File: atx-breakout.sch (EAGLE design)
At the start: 74 parts, among them Q1 IRF9530, Q2 IRF9530, Q3 IRF9530, Q4 IRF9530, Q5 IRF9530, Q6 IRF9530, T1 2N3904, T2 2N3904, T3 2N3904, T4 2N3904, T5 2N3904, T6 2N3904, X10 MA02-1JC, X12 XT30-J, X13 MA02-1JC, X15 XT30-J, X16 MA02-1JC, X2 XT30-J, X3 MA02-1JC, X4 XT30-J, X5 MA02-1JC, X6 XT30-J, X7 MA02-1JC, X9 XT30-J

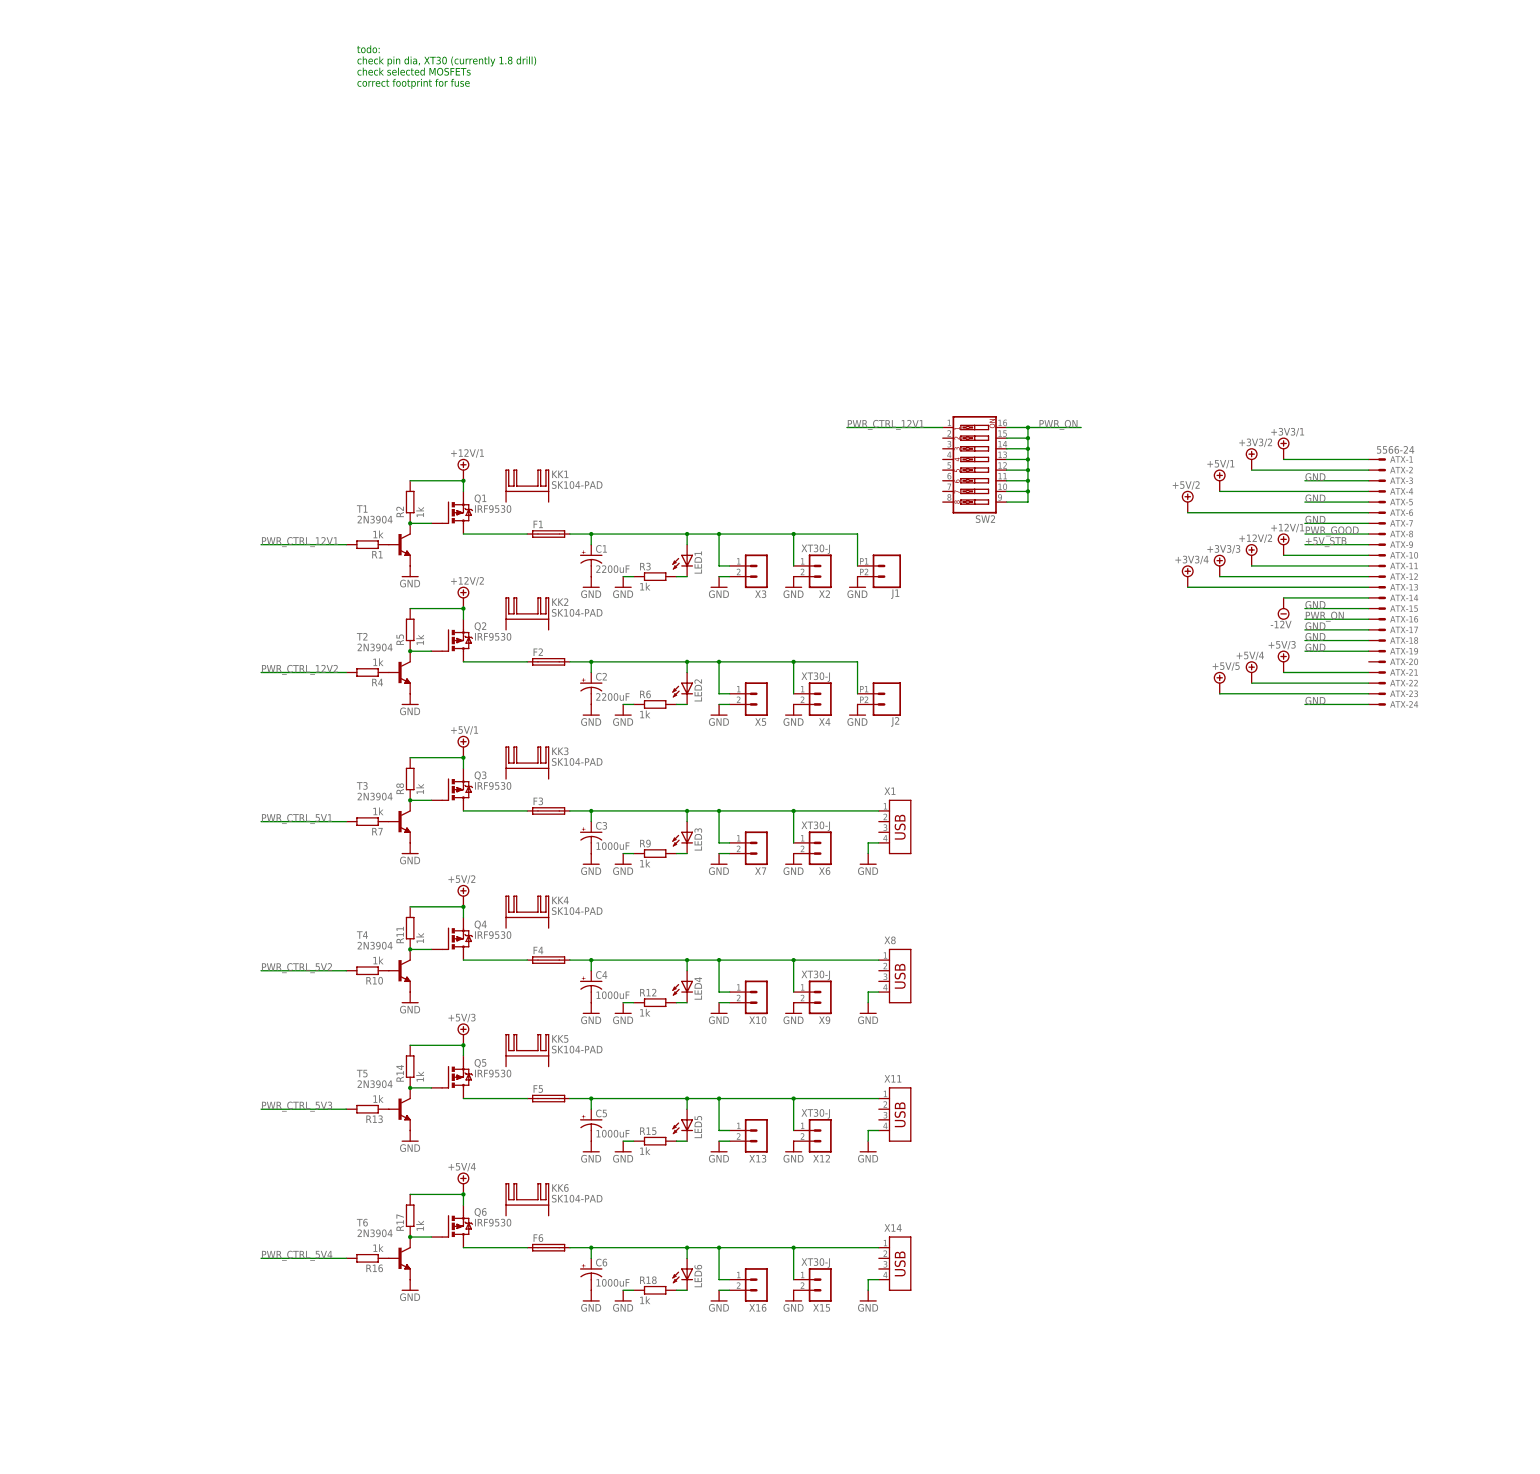
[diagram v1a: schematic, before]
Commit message: Added 3v3, control header, fan control headers, extra room for filter cap
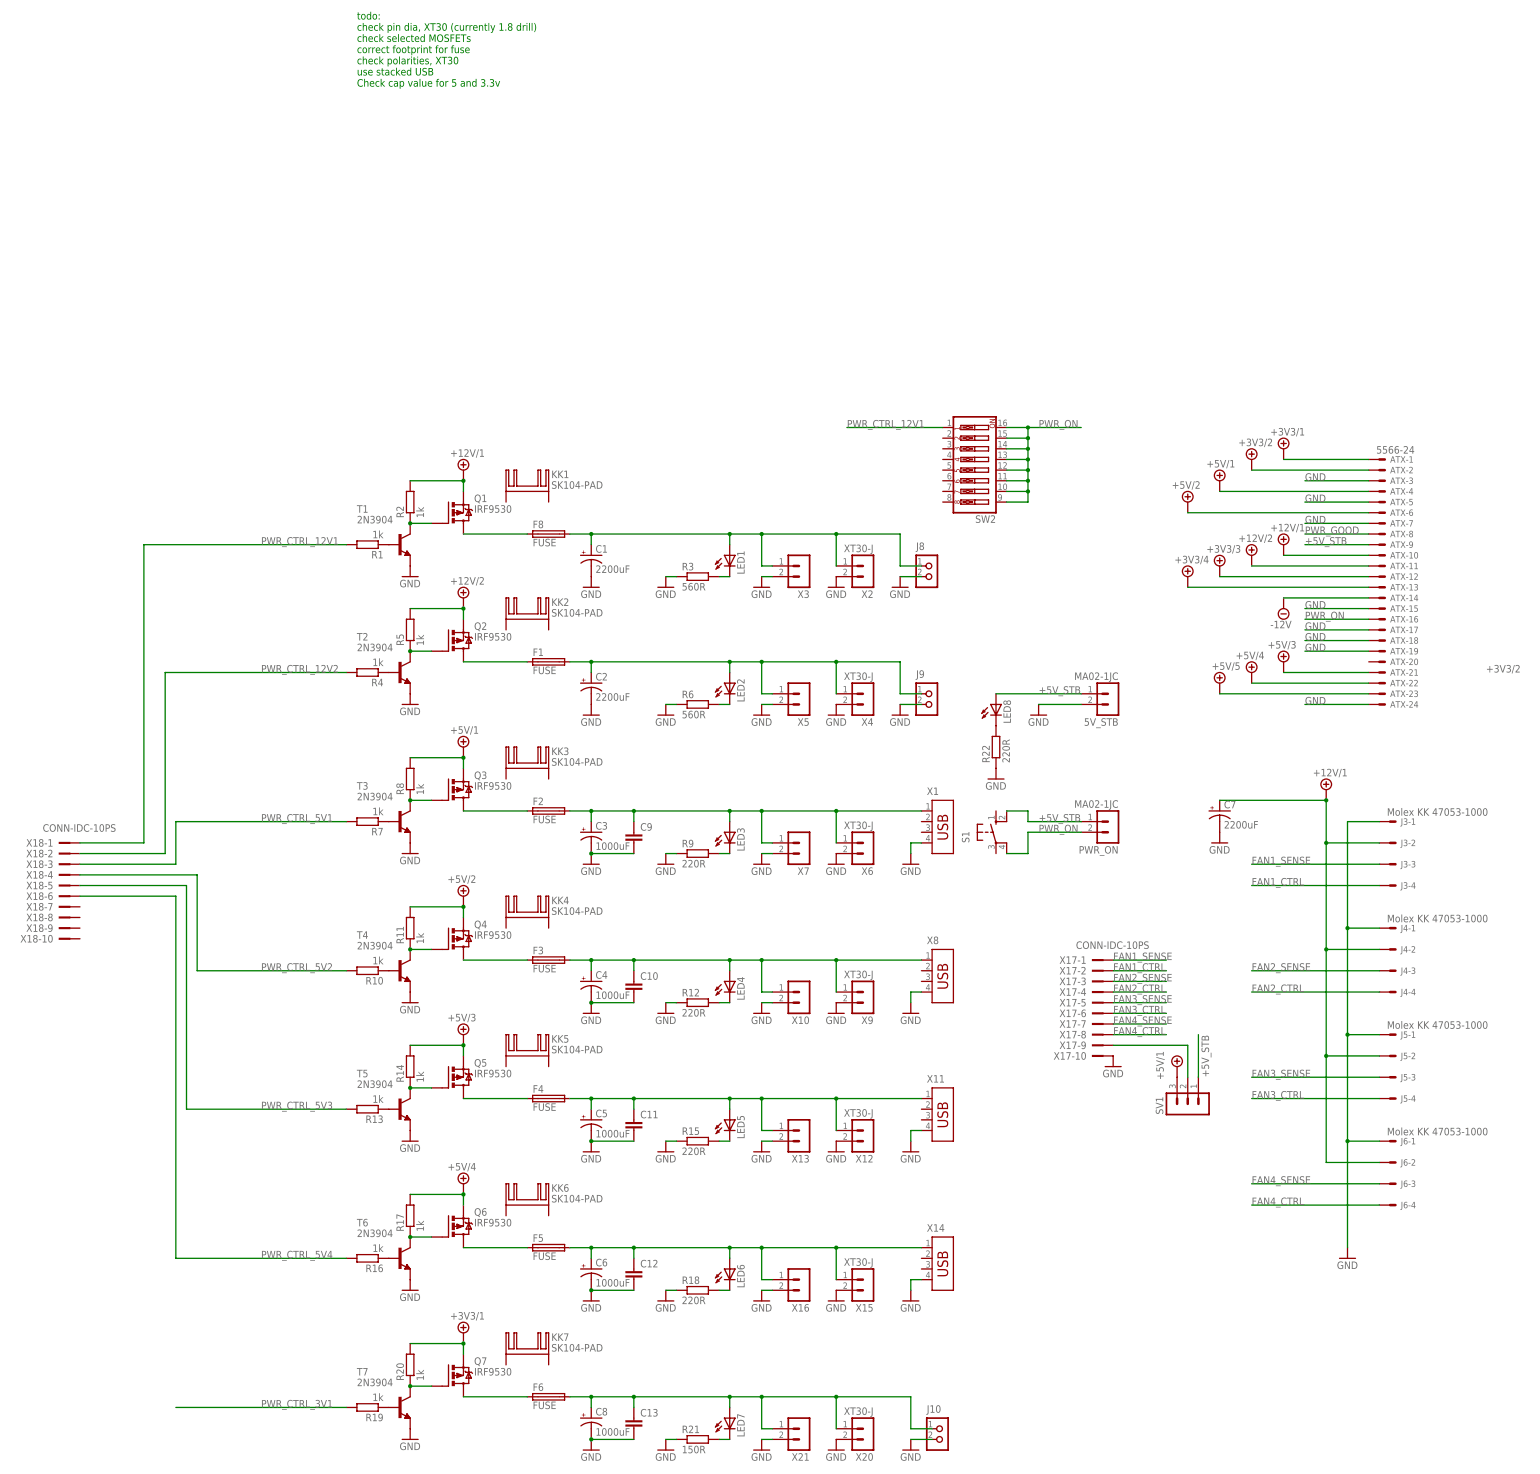
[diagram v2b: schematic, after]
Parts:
- removed J1, J2: (no value), SparkFun-Connectors:CONN_022.54MM_SCREWTERM
- added 5V_STB, PWR_ON, X21: MA02-1JC, joakim:MA02-1JC
- added C10, C11, C12, C13, C9: (no value), rcl:C-EU050-030X075
- added C7: 2200uF, rcl:CPOL-USE7.5-16
- added C8: 1000uF, rcl:CPOL-USE5-10.5
- added F8: FUSE, fuse:FUSEBLANK_5X20MM
- added J10, J8, J9: CON_TERMINAL_BLOCK_02-5MM, dp_devices.v6:CON_TERMINAL_BLOCK_02-5MM
- added J3, J4, J5, J6: Molex KK 47053-1000, con-molex:22-27-2041-04
- added KK7: SK104-PAD, heatsink:SK104-PAD
- added LED7, LED8: (no value), joakim:LED_J3MM
- added Q7: IRF9530, transistor-power:IRF9530
- added R19, R20: 1k, rcl:R-EU_0207/7
- added R21: 150R, rcl:R-EU_0207/7
- added R22: 220R, rcl:R-EU_0207/7
- added S1: (no value), joakim:PUSHBUTTON_12MM
- added SV1: (no value), joakim:MA03-1JC
- added T7: 2N3904, transistor:2N3904
- added X17, X18: CONN-IDC-10PS, joakim:CONN-IDC-10PS
- added X20: XT30-J, joakim:XT30-J
- F1, F2, F3, F4, F5, F6: value (none) -> FUSE; device fuse:LITTLEFUSE -> fuse:FUSEBLANK_5X20MM
- R12, R15, R18, R9: value 1k -> 220R
- R3, R6: value 1k -> 560R
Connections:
- new net +12V/1: ATX-10.S, C7.+, J3-2.S, J4-2.S, J5-2.S, J6-2.S, Q1.S, R2.2
- new net +12V/2: ATX-11.S, Q2.S, R5.2
- new net +3V3/1: ATX-1.S, Q7.S, R20.2
- new net +3V3/2: ATX-2.S
- new net +3V3/3: ATX-12.S
- new net +3V3/4: ATX-13.S
- new net FAN1_CTRL: J3-4.S, X17-2.KL
- new net FAN1_SENSE: J3-3.S, X17-1.KL
- new net FAN2_CTRL: J4-4.S, X17-4.KL
- new net FAN2_SENSE: J4-3.S, X17-3.KL
- new net FAN3_CTRL: J5-4.S, X17-6.KL
- new net FAN3_SENSE: J5-3.S, X17-5.KL
- new net FAN4_CTRL: J6-4.S, X17-8.KL
- new net FAN4_SENSE: J6-3.S, X17-7.KL
- new net N$32: SV1.2, X17-9.KL
- new net N$33: R19.1, T7.B
- new net N$34: Q7.G, R20.1, T7.C
- new net N$35: C13.1, C8.+, F6.2, J10.1, LED7.A, X20.1, X21.1
- new net N$36: LED7.C, R21.2
- new net N$37: F6.1, Q7.D
- new net PWR_CTRL_3V1: R19.2
- net +5V/1: now also SV1.3; no longer ATX-1.S, ATX-10.S, ATX-11.S, ATX-12.S, ATX-13.S, ATX-2.S, Q2.S, R5.2
- net +5V_STB: now also 5V_STB.1, LED8.A, PWR_ON.1, S1.S1, SV1.1
- net GND: now also 5V_STB.2, C10.2, C11.2, C12.2, C13.2, C7.-, C8.-, C9.2, J10.2, J3-1.S, J4-1.S, J5-1.S, J6-1.S, J8.2, J9.2, R21.1, R22.1, T7.E, X17-10.KL, X20.2, X21.2; no longer J1.2, J2.2
- net N$11: now also F1.1; no longer F2.1
- net N$14: now also C9.1, F2.2; no longer F3.2
- net N$16: now also F2.1; no longer F3.1
- net N$19: now also C10.1, F3.2; no longer F4.2
- net N$21: now also F3.1; no longer F4.1
- net N$24: now also C11.1, F4.2; no longer F5.2
- net N$26: now also F4.1; no longer F5.1
- net N$29: now also C12.1, F5.2; no longer F6.2
- net N$3: now also LED8.C, R22.2; no longer Q1.S, R2.2
- net N$31: now also F5.1; no longer F6.1
- net N$4: now also F8.2, J8.1; no longer F1.2, J1.1
- net N$6: now also F8.1; no longer F1.1
- net N$9: now also F1.2, J9.1; no longer F2.2, J2.1
- net PWR_CTRL_12V1: now also X18-1.KL
- net PWR_CTRL_12V2: now also X18-2.KL
- net PWR_CTRL_5V1: now also X18-3.KL
- net PWR_CTRL_5V2: now also X18-4.KL
- net PWR_CTRL_5V3: now also X18-5.KL
- net PWR_CTRL_5V4: now also X18-6.KL
- net PWR_ON: now also PWR_ON.2, S1.P1
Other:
- note added: "todo: check pin dia, XT30 (currently 1.8 drill) check selected MOSFETs correct footprint for fuse check polarities, XT30 use stacked USB Check cap value for 5 and 3.3v"
- note removed: "todo: check pin dia, XT30 (currently 1.8 drill) check selected MOSFETs correct footprint for fuse"
- moved on the sheet: LED1, LED2, LED3, LED4, LED5, LED6, R12, R15, R18, R3, R6, R9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

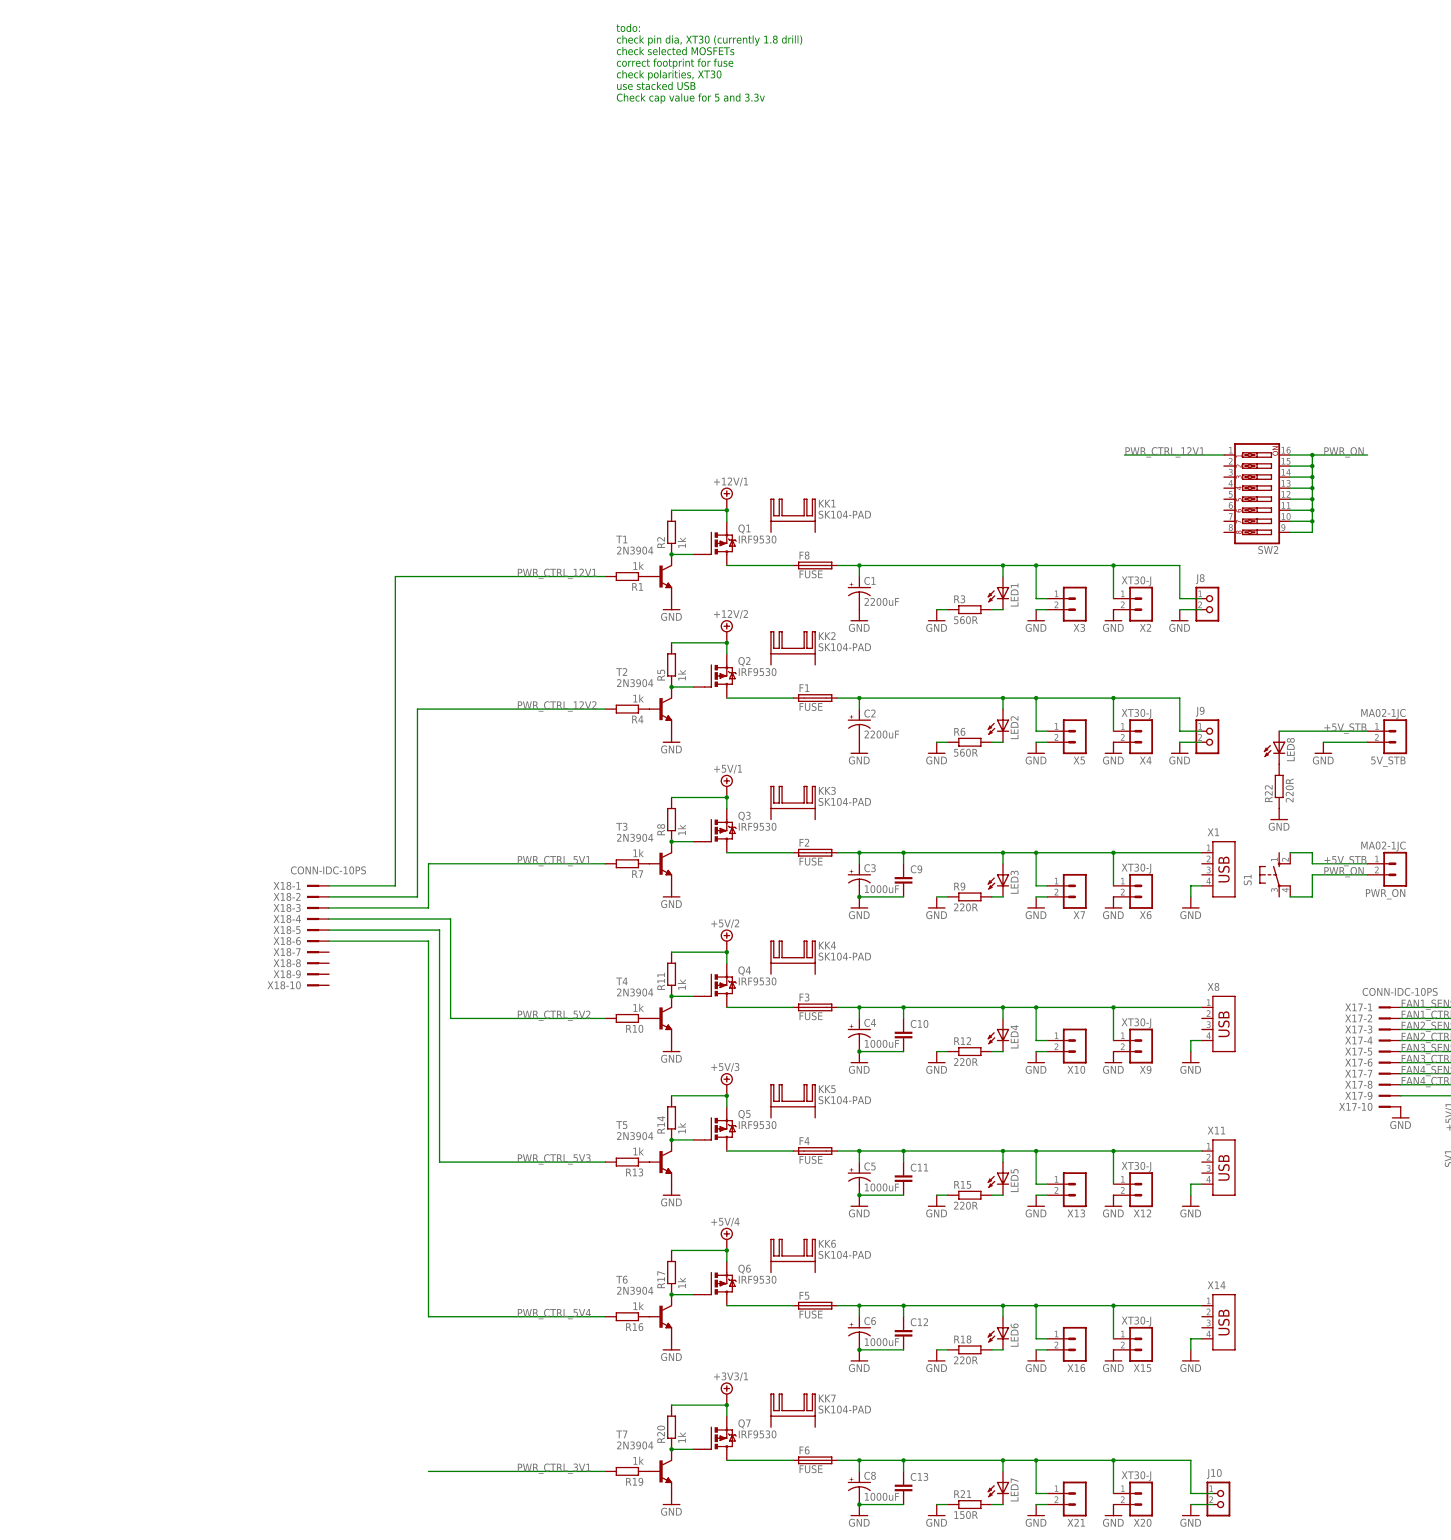
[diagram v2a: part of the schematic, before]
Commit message: More cleanup, made room for screws etc
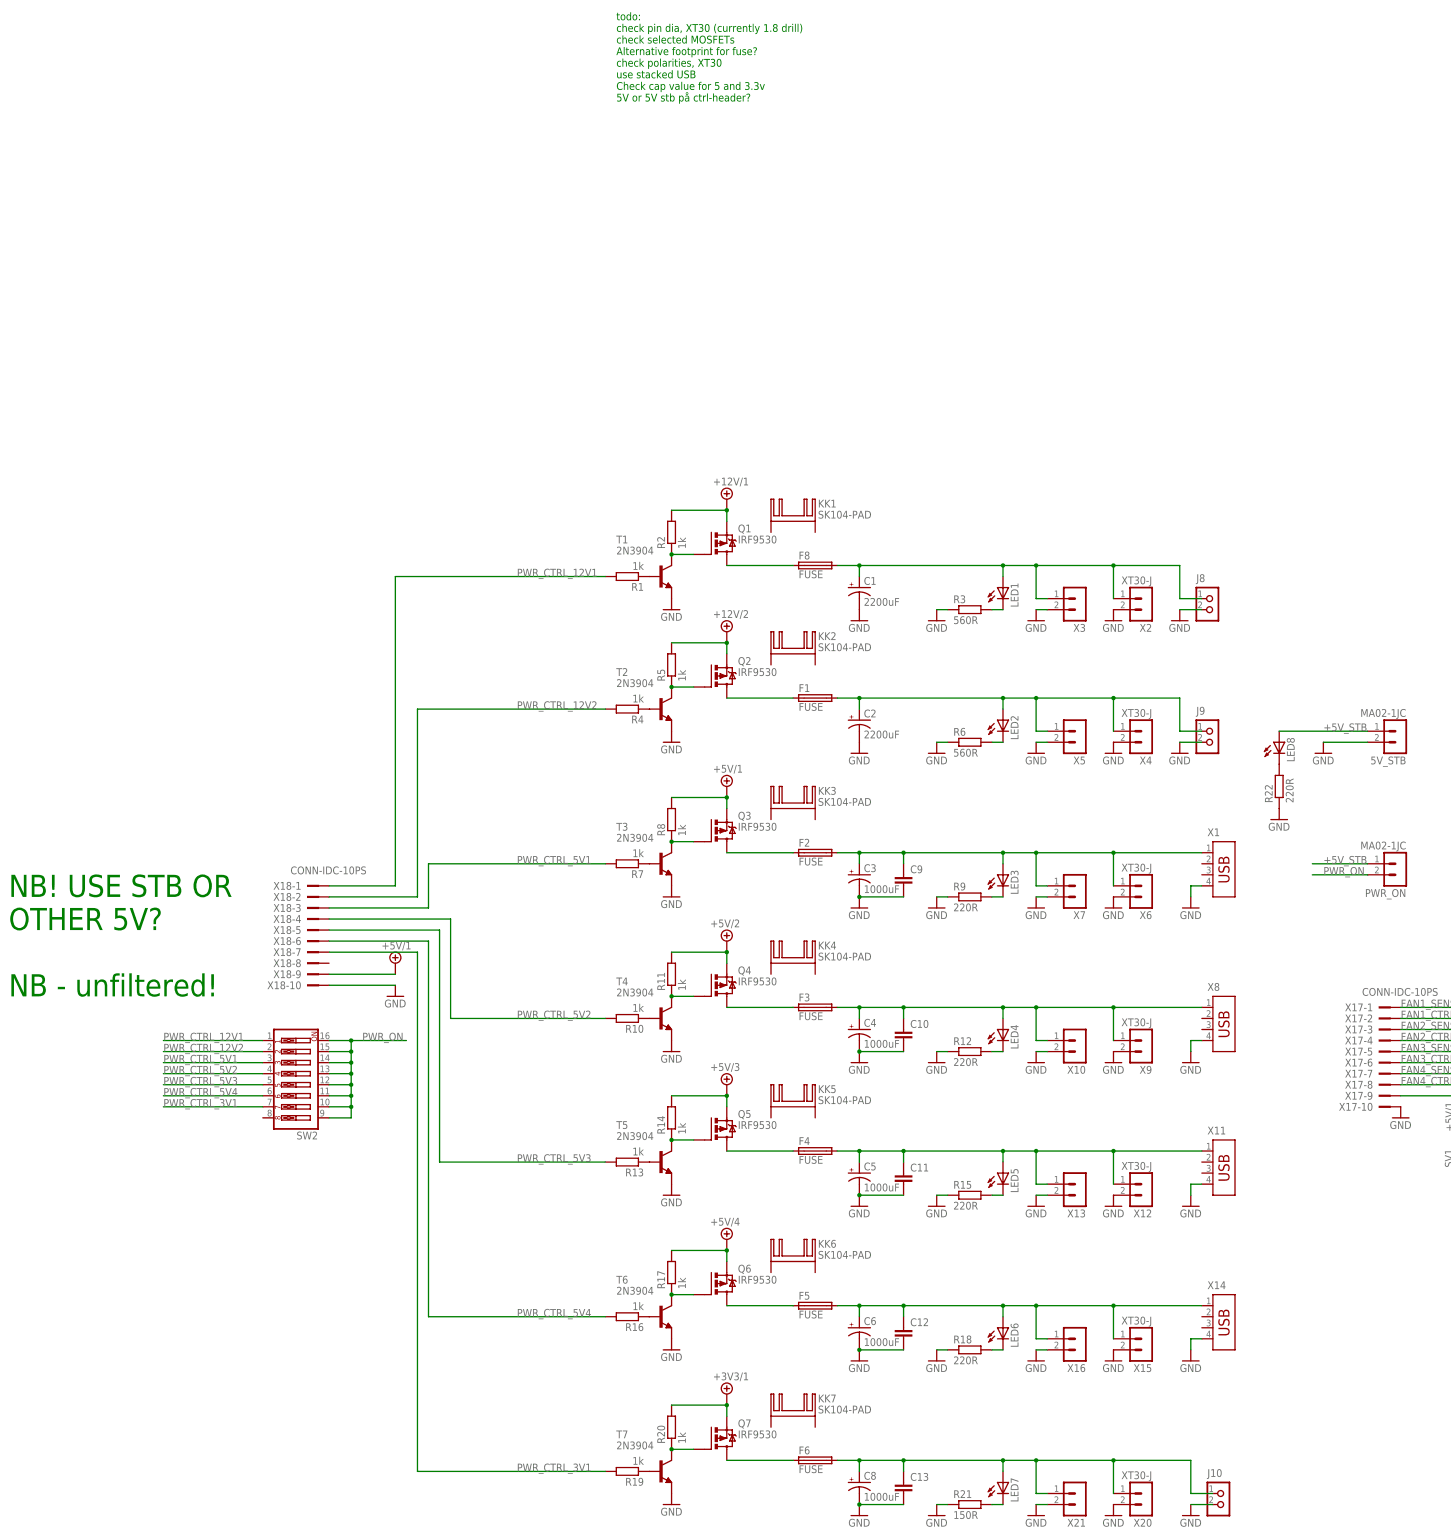
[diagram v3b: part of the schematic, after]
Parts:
- removed S1: (no value), joakim:PUSHBUTTON_12MM
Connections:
- net +5V/1: now also X18-9.KL
- net +5V_STB: no longer S1.S1
- net GND: now also X18-10.KL
- net PWR_CTRL_12V2: now also SW2.2
- net PWR_CTRL_3V1: now also SW2.7, X18-7.KL
- net PWR_CTRL_5V1: now also SW2.3
- net PWR_CTRL_5V2: now also SW2.4
- net PWR_CTRL_5V3: now also SW2.5
- net PWR_CTRL_5V4: now also SW2.6
- net PWR_ON: no longer S1.P1
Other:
- note added: "NB! USE STB OR OTHER 5V? NB - unfiltered!"
- note added: "todo: check pin dia, XT30 (currently 1.8 drill) check selected MOSFETs Alternative footprint for fuse? check polarities, XT30 use stacked USB Check cap value for 5 and 3.3v 5V or 5V stb på ctrl-header?"
- note removed: "todo: check pin dia, XT30 (currently 1.8 drill) check selected MOSFETs correct footprint for fuse check polarities, XT30 use stacked USB Check cap value for 5 and 3.3v"
- moved on the sheet: SW2
